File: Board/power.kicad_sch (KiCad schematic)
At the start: 19 parts, among them U2 MP2459, U3 LMR516x5

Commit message: Routing mostly done
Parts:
- added C13: 22uF/30V, Capacitor_SMD:C_0603_1608Metric, symbol Device:C_Small
- added C14, C9: 100n/100V, Capacitor_SMD:C_0603_1608Metric, symbol Device:C_Small
- added C15, C16, C8: 1µF/100V, Capacitor_SMD:C_0603_1608Metric, symbol Device:C_Small
- added D6: 1N4007, Diode_SMD:D_SOD-123, symbol Device:D_Small
- added L2: 24.5uH, symbol Device:L
- added R10: 3.48k 0.1%, Resistor_SMD:R_0603_1608Metric, symbol Device:R_Small
- added R8: 100k 0.1%, Resistor_SMD:R_0603_1608Metric, symbol Device:R_Small
- C7: value 22u -> 22uF/30V
- U3: value LMR516x5 -> LMR51635XDDCR
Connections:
- net +24V: now also C13.1, L2.2, R8.1
- net GND: now also U3.4 (GND), C13.2, C14.2, C15.2, C16.2, C8.2, R10.2
- net at U3.1 (FB): now also R10.1, R8.2
- net at U3.2 (EN): now also U3.3 (VIN), C14.1, C15.1, C16.1, C8.1, D6.1 (K)
- net at U3.5 (SW): now also C9.2, L2.1
- net at U3.6 (CB): now also C9.1
- new net VIN: D6.2 (A)
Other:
- note added: "24V SUPPLY"
- note added: "VIN range from 40V to 55V approx."
- note removed: "VIN range from 12V to 60V approx."
- moved on the sheet: C1, C11, C2, C6, C7, D1, D3, D4, D5, FB4, L1, R16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

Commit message: Schematic done.
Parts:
- removed D1: 1N4007, Diode_SMD:D_SOD-123, symbol Device:D_Small
- D6: value 1N4007 -> SE30AFBHM3/6A; footprint Diode_SMD:D_SOD-123 -> Diode_SMD:D_SMA_Handsoldering; REF SM4007PL -> SE30AFBHM3/6A
- L1: REF NLCV25T-220K-PF -> NLCV25T-220K-EFD
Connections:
- net +24V: now also C1.1, C2.1, R3.1, U2.5 (IN)
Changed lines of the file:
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@@
 	)
 	(junction
-		(at 44.45 95.25)
-		(diameter 0)
-		(color 0 0 0 0)
-	)
-	(junction
 		(at 55.88 55.88)
 		(diameter 0)
@@
 	(wire
 		(pts
-			(xy 26.67 95.25) (xy 27.94 95.25)
+			(xy 26.67 95.25) (xy 36.83 95.25)
 		)
 		(stroke
@@
 		)
 	)
+	(wire
+		(pts
+			(xy 110.49 39.37) (xy 116.84 39.37)
+		)
+		(stroke
+			(width 0)
+			(type default)
+		)
+	)
 	(polyline
 		(pts
@@
 	(wire
 		(pts
-			(xy 110.49 39.37) (xy 116.84 39.37)
-		)
-		(stroke
-			(width 0)
-			(type default)
-		)
-	)
-	(wire
-		(pts
 			(xy 165.1 101.6) (xy 167.64 101.6)
 		)
@@
 	(wire
 		(pts
-			(xy 36.83 95.25) (xy 44.45 95.25)
+			(xy 36.83 95.25) (xy 52.07 95.25)
 		)
 		(stroke
@@
 		)
 	)
-	(wire
-		(pts
-			(xy 33.02 95.25) (xy 36.83 95.25)
-		)
-		(stroke
-			(width 0)
-			(type default)
-		)
-	)
 	(polyline
 		(pts
@@
 	(wire
 		(pts
-			(xy 44.45 95.25) (xy 52.07 95.25)
-		)
-		(stroke
-			(width 0)
-			(type default)
-		)
-	)
-	(wire
-		(pts
 			(xy 64.77 48.26) (xy 64.77 55.88)
 		)
@@
 			)
 		)
-		(property "REF" "NLCV25T-220K-PF"
+		(property "REF" "NLCV25T-220K-EFD"
 			(at 127 101.6 90)
 			(effects
@@
 	)
 	(symbol
-		(lib_id "power:PWR_FLAG")
-		(at 44.45 95.25 0)
-		(unit 1)
-		(exclude_from_sim no)
-		(in_bom yes)
-		(on_board yes)
-		(dnp no)
-		(fields_autoplaced yes)
-		(property "Reference" "#FLG05"
-			(at 44.45 93.345 0)
-			(effects
-				(font
-					(size 1.27 1.27)
-				)
-				(hide yes)
-			)
-		)
-		(property "Value" "PWR_FLAG"
-			(at 44.45 91.1169 0)
-			(effects
-				(font
-					(size 1.27 1.27)
-				)
-			)
-		)
-		(property "Footprint" ""
-			(at 44.45 95.25 0)
-			(effects
-				(font
-					(size 1.27 1.27)
-				)
-				(hide yes)
-			)
-		)
-		(property "Datasheet" "~"
-			(at 44.45 95.25 0)
-			(effects
-				(font
-					(size 1.27 1.27)
-				)
-				(hide yes)
-			)
-		)
-		(property "Description" "Special symbol for telling ERC where power comes from"
-			(at 44.45 95.25 0)
-			(effects
-				(font
-					(size 1.27 1.27)
-				)
-				(hide yes)
-			)
-		)
-		(pin "1"
-		)
-		(instances
-			(project "linear_act_controller"
-				(path "/a7f12679-28d2-4dcb-a620-9ebf42b92b51/9aa0f8d5-db02-4fb8-86c3-5f9e7fcbafc5"
-					(reference "#FLG05")
-					(unit 1)
-				)
-			)
-		)
-	)
-	(symbol
 		(lib_id "Device:D_Small")
 		(at 35.56 36.83 180)
@@
 			)
 		)
-		(property "Value" "1N4007"
+		(property "Value" "SE30AFBHM3/6A"
 			(at 35.56 39.7256 0)
 			(effects
@@
 			)
 		)
-		(property "Footprint" "Diode_SMD:D_SOD-123"
+		(property "Footprint" "Diode_SMD:D_SMA_Handsoldering"
 			(at 35.56 36.83 90)
 			(effects
@@
 			)
 		)
-		(property "REF" "SM4007PL"
+		(property "REF" "SE30AFBHM3/6A"
 			(at 35.56 36.83 0)
 			(effects
@@
 					(unit 1)
 				)
-			)
-		)
-	)
-	(symbol
-		(lib_id "Device:D_Small")
-		(at 30.48 95.25 180)
-		(unit 1)
-		(exclude_from_sim no)
-		(in_bom yes)
-		(on_board yes)
-		(dnp no)
-		(property "Reference" "D1"
-			(at 30.48 100.457 0)
-			(effects
-				(font
-					(size 1.27 1.27)
-				)
-			)
-		)
-		(property "Value" "1N4007"
-			(at 30.48 98.1456 0)
-			(effects
-				(font
-					(size 1.27 1.27)
-				)
-			)
-		)
-		(property "Footprint" "Diode_SMD:D_SOD-123"
-			(at 30.48 95.25 90)
-			(effects
-				(font
-					(size 1.27 1.27)
-				)
-				(hide yes)
-			)
-		)
-		(property "Datasheet" "~"
-			(at 30.48 95.25 90)
-			(effects
-				(font
-					(size 1.27 1.27)
-				)
-				(hide yes)
-			)
-		)
-		(property "Description" "Diode, small symbol"
-			(at 30.48 95.25 0)
-			(effects
-				(font
-					(size 1.27 1.27)
-				)
-				(hide yes)
-			)
-		)
-		(property "REF" "SM4007PL"
-			(at 30.48 95.25 0)
-			(effects
-				(font
-					(size 1.27 1.27)
-				)
-				(hide yes)
-			)
-		)
-		(property "RS" ""
-			(at 30.48 95.25 0)
-			(effects
-				(font
-					(size 1.27 1.27)
-				)
-				(hide yes)
-			)
-		)
-		(property "JLCPCB" "C64898"
-			(at 30.48 95.25 0)
-			(effects
-				(font
-					(size 1.27 1.27)
-				)
-				(hide yes)
-			)
-		)
-		(property "Sim.Device" "D"
-			(at 30.48 95.25 0)
-			(effects
-				(font
-					(size 1.27 1.27)
-				)
-				(hide yes)
-			)
-		)
-		(property "Sim.Pins" "1=K 2=A"
-			(at 30.48 95.25 0)
-			(effects
-				(font
-					(size 1.27 1.27)
-				)
-				(hide yes)
-			)
-		)
-		(pin "1"
-		)
-		(pin "2"
-		)
-		(instances
-			(project "linear_act_controller"
-				(path "/a7f12679-28d2-4dcb-a620-9ebf42b92b51/9aa0f8d5-db02-4fb8-86c3-5f9e7fcbafc5"
-					(reference "D1")
-					(unit 1)
-				)

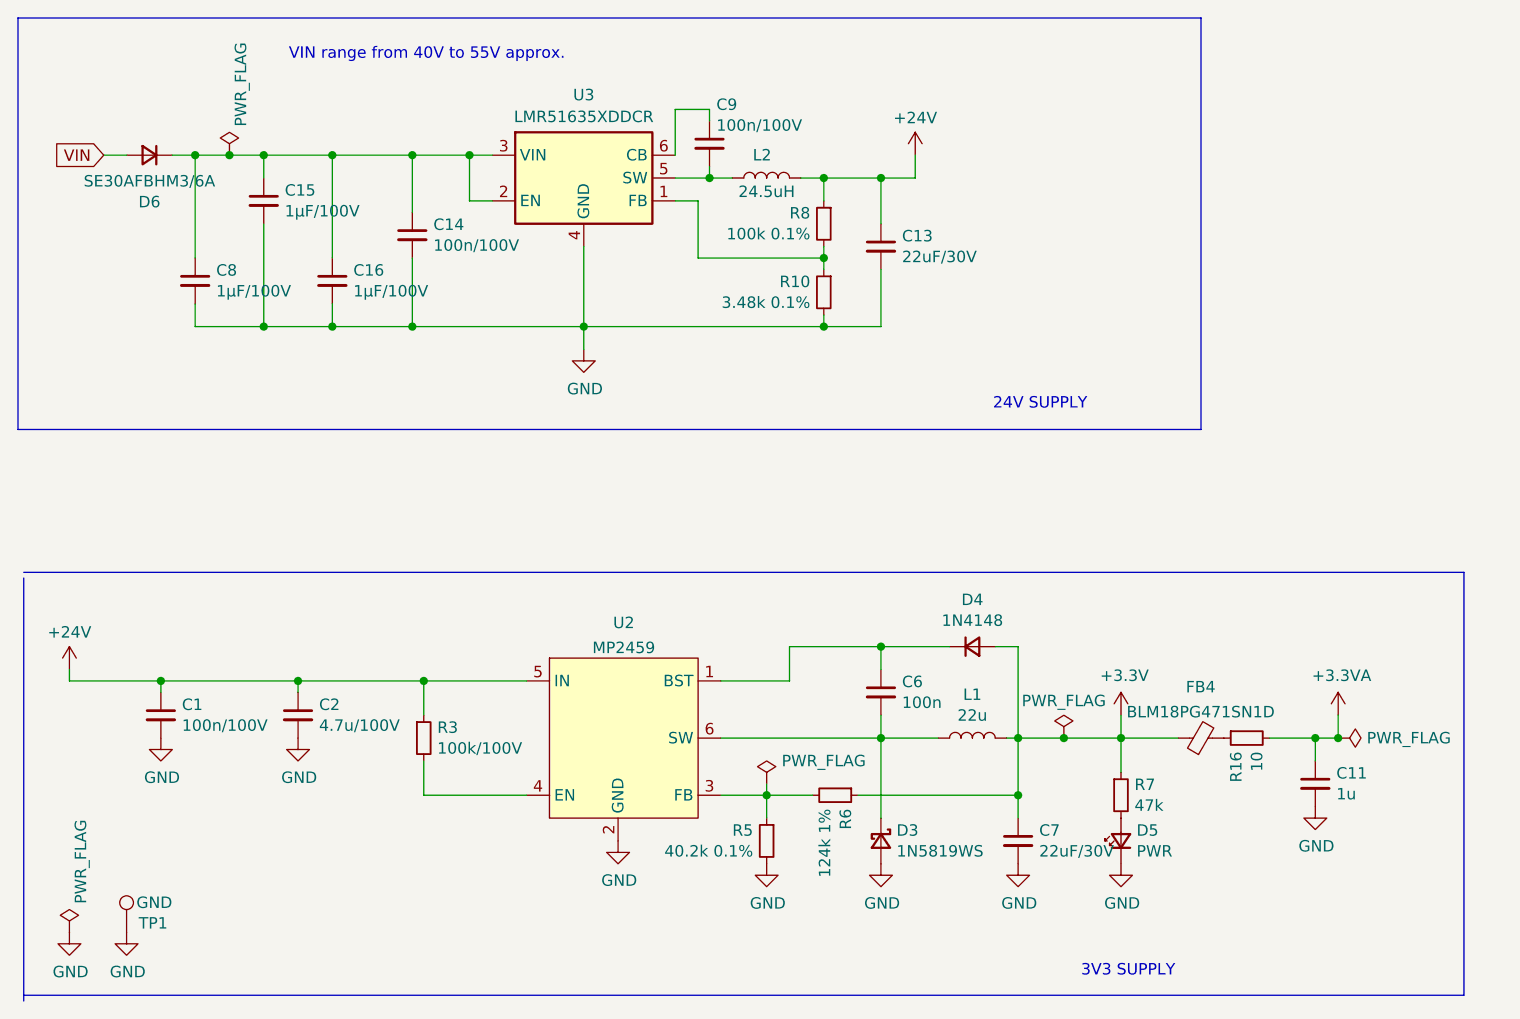
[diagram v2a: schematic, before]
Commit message: Included jdam's improvements.
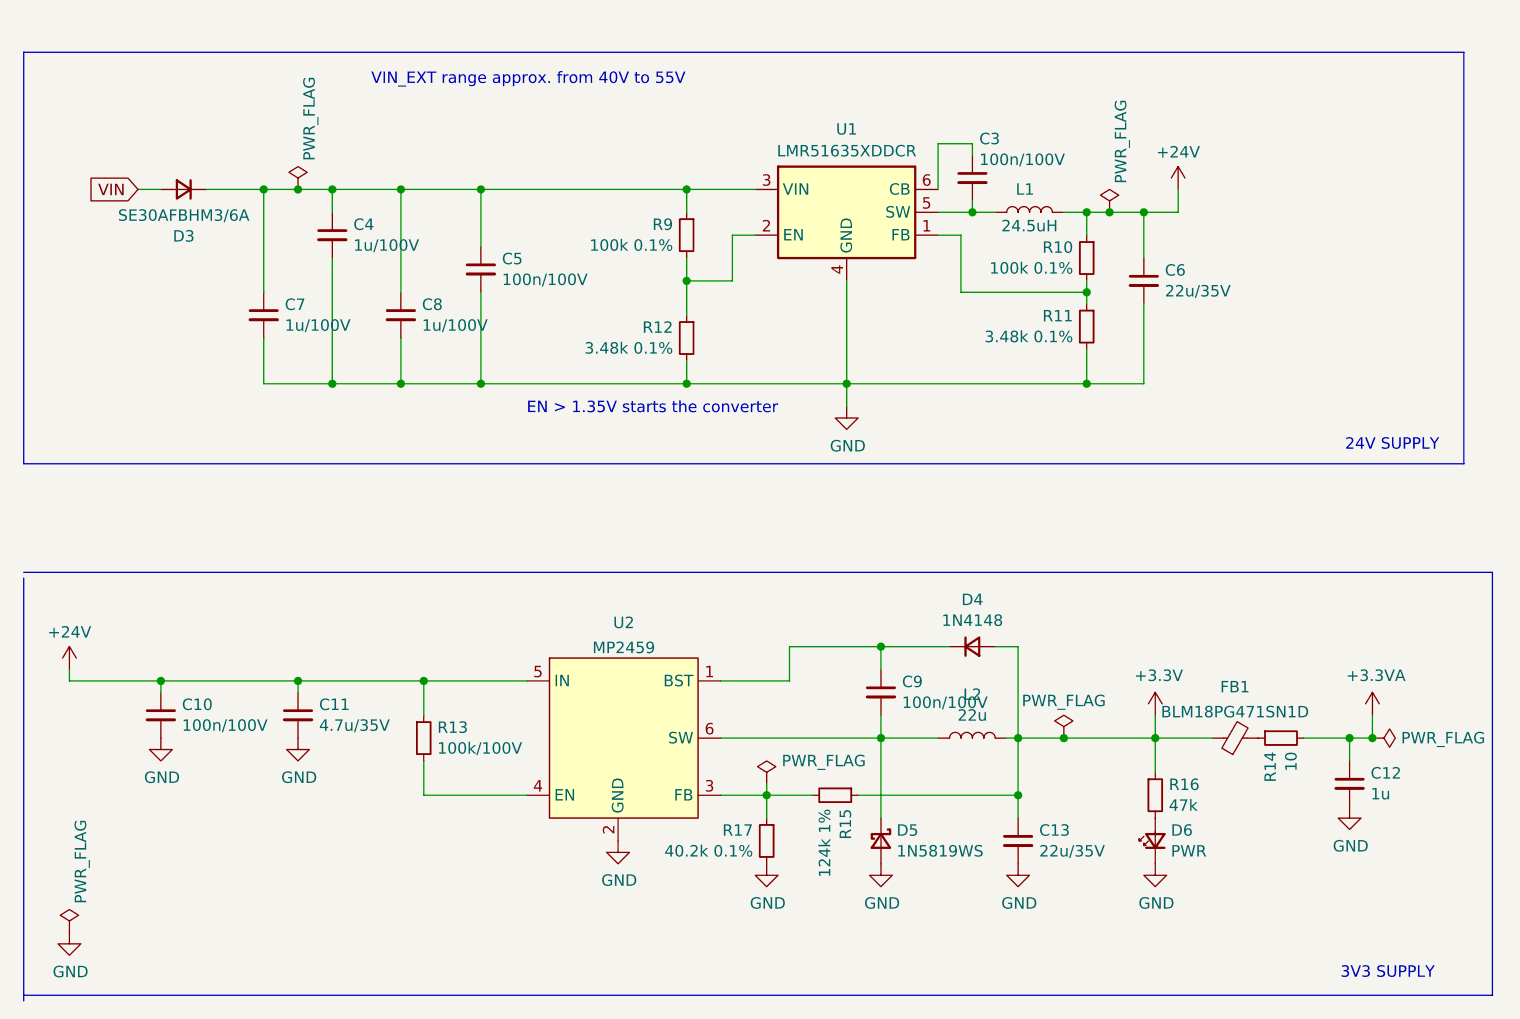
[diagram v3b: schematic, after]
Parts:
- removed TP1: GND, TestPoint:TestPoint_Pad_D1.0mm, symbol Connector:TestPoint
- added R12: 3.48k 0.1%, Resistor_SMD:R_0603_1608Metric_Pad0.98x0.95mm_HandSolder, symbol Device:R_Small
- added R9: 100k 0.1%, Resistor_SMD:R_0603_1608Metric_Pad0.98x0.95mm_HandSolder, symbol Device:R_Small
- C10: renamed from C1; footprint Capacitor_SMD:C_0603_1608Metric -> Capacitor_SMD:C_0603_1608Metric_Pad1.08x0.95mm_HandSolder
- C11: renamed from C2; value 4.7u/100V -> 4.7u/35V; footprint Capacitor_SMD:C_1206_3216Metric -> Capacitor_SMD:C_0603_1608Metric_Pad1.08x0.95mm_HandSolder; REF HMK325C7475KMHPE -> (none)
- C12: renamed from C11; footprint Capacitor_SMD:C_0603_1608Metric -> Capacitor_SMD:C_0603_1608Metric_Pad1.08x0.95mm_HandSolder
- C13: renamed from C7; value 22uF/30V -> 22u/35V; footprint Capacitor_SMD:C_1206_3216Metric -> Capacitor_SMD:C_0805_2012Metric_Pad1.18x1.45mm_HandSolder; REF JMK316AB7226KLHT -> (none)
- C3: renamed from C9; footprint Capacitor_SMD:C_0603_1608Metric -> Capacitor_SMD:C_0603_1608Metric_Pad1.08x0.95mm_HandSolder
- C4: renamed from C15; value 1µF/100V -> 1u/100V; footprint Capacitor_SMD:C_0603_1608Metric -> Capacitor_SMD:C_0603_1608Metric_Pad1.08x0.95mm_HandSolder
- C5: renamed from C14; footprint Capacitor_SMD:C_0603_1608Metric -> Capacitor_SMD:C_0603_1608Metric_Pad1.08x0.95mm_HandSolder
- C6: renamed from C13; value 22uF/30V -> 22u/35V; footprint Capacitor_SMD:C_0603_1608Metric -> Capacitor_SMD:C_0805_2012Metric_Pad1.18x1.45mm_HandSolder
- C7: renamed from C8; value 1µF/100V -> 1u/100V; footprint Capacitor_SMD:C_0603_1608Metric -> Capacitor_SMD:C_0603_1608Metric_Pad1.08x0.95mm_HandSolder
- C8: renamed from C16; value 1µF/100V -> 1u/100V; footprint Capacitor_SMD:C_0603_1608Metric -> Capacitor_SMD:C_0603_1608Metric_Pad1.08x0.95mm_HandSolder
- C9: renamed from C6; value 100n -> 100n/100V; footprint Capacitor_SMD:C_0603_1608Metric -> Capacitor_SMD:C_0603_1608Metric_Pad1.08x0.95mm_HandSolder
- D4: footprint Diode_SMD:D_SOD-323 -> Diode_SMD:D_SOD-323_HandSoldering
- D5: renamed from D3; footprint Diode_SMD:D_SOD-323 -> Diode_SMD:D_SOD-323_HandSoldering
- D6: renamed from D5; footprint LED_SMD:LED_0603_1608Metric -> LED_SMD:LED_0603_1608Metric_Pad1.05x0.95mm_HandSolder
- L1: renamed from L2; footprint (none) -> Inductors:Pulse_PG1083.253NLT
- R10: renamed from R8; footprint Resistor_SMD:R_0603_1608Metric -> Resistor_SMD:R_0603_1608Metric_Pad0.98x0.95mm_HandSolder
- R11: renamed from R10; footprint Resistor_SMD:R_0603_1608Metric -> Resistor_SMD:R_0603_1608Metric_Pad0.98x0.95mm_HandSolder
- R13: renamed from R3; footprint Resistor_SMD:R_0603_1608Metric -> Resistor_SMD:R_0603_1608Metric_Pad0.98x0.95mm_HandSolder
- R14: renamed from R16; footprint Resistor_SMD:R_0603_1608Metric -> Resistor_SMD:R_0603_1608Metric_Pad0.98x0.95mm_HandSolder
- R15: renamed from R6; footprint Resistor_SMD:R_0603_1608Metric -> Resistor_SMD:R_0603_1608Metric_Pad0.98x0.95mm_HandSolder
- R16: renamed from R7; footprint Resistor_SMD:R_0603_1608Metric -> Resistor_SMD:R_0603_1608Metric_Pad0.98x0.95mm_HandSolder
- R17: renamed from R5; footprint Resistor_SMD:R_0603_1608Metric -> Resistor_SMD:R_0603_1608Metric_Pad0.98x0.95mm_HandSolder
- renumbered D6 to D3, FB4 to FB1, L1 to L2, U3 to U1
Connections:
- net GND: now also R12.2
- net at C4.1, C5.1, C7.1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: now also R9.1; no longer U1.2 (EN)
- new net: R12.1, R9.2, U1.2 (EN)
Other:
- note added: "EN > 1.35V starts the converter"
- note added: "VIN_EXT range approx. from 40V to 55V"
- note removed: "VIN range from 40V to 55V approx."
- moved on the sheet: C12, C3, C4, C5, C6, C7, C8, D3, D6, FB1, L1, R10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

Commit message: WIP on routing
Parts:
- removed D6: PWR, LED_SMD:LED_0603_1608Metric_Pad1.05x0.95mm_HandSolder, symbol Device:LED_Small
- removed R16: 47k, Resistor_SMD:R_0603_1608Metric_Pad0.98x0.95mm_HandSolder, symbol Device:R_Small
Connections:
- net +24V: now also L1.1; no longer L1.2
- net at C3.2, U1.5 (SW): now also L1.2; no longer L1.1
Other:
- moved on the sheet: L1
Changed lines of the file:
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@@
 	(wire
 		(pts
-			(xy 147.32 101.6) (xy 147.32 105.41)
-		)
-		(stroke
-			(width 0)
-			(type default)
-		)
-	)
-	(wire
-		(pts
 			(xy 116.84 101.6) (xy 116.84 99.06)
 		)
@@
 	)
 	(symbol
-		(lib_id "power:GND")
-		(at 147.32 115.57 0)
-		(unit 1)
-		(exclude_from_sim no)
-		(in_bom yes)
-		(on_board yes)
-		(dnp no)
-		(property "Reference" "#PWR018"
-			(at 147.32 121.92 0)
-			(effects
-				(font
-					(size 1.27 1.27)
-				)
-				(hide yes)
-			)
-		)
-		(property "Value" "GND"
-			(at 147.447 119.9642 0)
-			(effects
-				(font
-					(size 1.27 1.27)
-				)
-			)
-		)
-		(property "Footprint" ""
-			(at 147.32 115.57 0)
-			(effects
-				(font
-					(size 1.27 1.27)
-				)
-				(hide yes)
-			)
-		)
-		(property "Datasheet" ""
-			(at 147.32 115.57 0)
-			(effects
-				(font
-					(size 1.27 1.27)
-				)
-				(hide yes)
-			)
-		)
-		(property "Description" "Power symbol creates a global label with name \"GND\" , ground"
-			(at 147.32 115.57 0)
-			(effects
-				(font
-					(size 1.27 1.27)
-				)
-				(hide yes)
-			)
-		)
-		(pin "1"
-		)
-		(instances
-			(project "linear_act_controller"
-				(path "/a7f12679-28d2-4dcb-a620-9ebf42b92b51/9aa0f8d5-db02-4fb8-86c3-5f9e7fcbafc5"
-					(reference "#PWR018")
-					(unit 1)
-				)
-			)
-		)
-	)
-	(symbol
 		(lib_id "power:PWR_FLAG")
 		(at 142.24 43.18 0)
@@
 	(symbol
 		(lib_id "Device:L")
-		(at 133.35 43.18 90)
+		(at 133.35 43.18 270)
 		(unit 1)
 		(exclude_from_sim no)
@@
 		(dnp no)
 		(property "Reference" "L1"
-			(at 132.842 40.64 90)
+			(at 133.35 45.212 90)
 			(effects
 				(font
@@
 		)
 		(property "Value" "24.5uH"
-			(at 133.35 44.704 90)
+			(at 133.35 41.656 90)
 			(effects
 				(font
@@
 	)
 	(symbol
-		(lib_id "Device:R_Small")
-		(at 147.32 107.95 0)
-		(unit 1)
-		(exclude_from_sim no)
-		(in_bom yes)
-		(on_board yes)
-		(dnp no)
-		(property "Reference" "R16"
-			(at 148.8186 106.7816 0)
-			(effects
-				(font
-					(size 1.27 1.27)
-				)
-				(justify left)
-			)
-		)
-		(property "Value" "47k"
-			(at 148.8186 109.093 0)
-			(effects
-				(font
-					(size 1.27 1.27)
-				)
-				(justify left)
-			)
-		)
-		(property "Footprint" "Resistor_SMD:R_0603_1608Metric_Pad0.98x0.95mm_HandSolder"
-			(at 147.32 107.95 0)
-			(effects
-				(font
-					(size 1.27 1.27)
-				)
-				(hide yes)
-			)
-		)
-		(property "Datasheet" "~"
-			(at 147.32 107.95 0)
-			(effects
-				(font
-					(size 1.27 1.27)
-				)
-				(hide yes)
-			)
-		)
-		(property "Description" "Resistor, small symbol"
-			(at 147.32 107.95 0)
-			(effects
-				(font
-					(size 1.27 1.27)
-				)
-				(hide yes)
-			)
-		)
-		(pin "1"
-		)
-		(pin "2"
-		)
-		(instances
-			(project "linear_act_controller"
-				(path "/a7f12679-28d2-4dcb-a620-9ebf42b92b51/9aa0f8d5-db02-4fb8-86c3-5f9e7fcbafc5"
-					(reference "R16")
-					(unit 1)
-				)
-			)
-		)
-	)
-	(symbol
 		(lib_id "Device:C_Small")
 		(at 127 39.37 0)
@@
 					(unit 1)
 				)
-			)
-		)
-	)
-	(symbol
-		(lib_id "Device:LED_Small")
-		(at 147.32 113.03 90)
-		(unit 1)
-		(exclude_from_sim no)
-		(in_bom yes)
-		(on_board yes)
-		(dnp no)
-		(property "Reference" "D6"
-			(at 149.0472 111.8616 90)
-			(effects
-				(font
-					(size 1.27 1.27)
-				)
-				(justify right)
-			)
-		)
-		(property "Value" "PWR"
-			(at 149.0472 114.173 90)
-			(effects
-				(font
-					(size 1.27 1.27)
-				)
-				(justify right)
-			)
-		)
-		(property "Footprint" "LED_SMD:LED_0603_1608Metric_Pad1.05x0.95mm_HandSolder"
-			(at 147.32 113.03 90)
-			(effects
-				(font
-					(size 1.27 1.27)
-				)
-				(hide yes)
-			)
-		)
-		(property "Datasheet" "~"
-			(at 147.32 113.03 90)
-			(effects
-				(font
-					(size 1.27 1.27)
-				)
-				(hide yes)
-			)
-		)
-		(property "Description" "Light emitting diode, small symbol"
-			(at 147.32 113.03 0)
-			(effects
-				(font
-					(size 1.27 1.27)
-				)
-				(hide yes)
-			)
-		)
-		(property "Sim.Pin" "1=K 2=A"
-			(at 147.32 113.03 0)
-			(effects
-				(font
-					(size 1.27 1.27)
-				)
-				(hide yes)
-			)
-		)
-		(pin "1"
-		)
-		(pin "2"
-		)
-		(instances
-			(project "linear_act_controller"
-				(path "/a7f12679-28d2-4dcb-a620-9ebf42b92b51/9aa0f8d5-db02-4fb8-86c3-5f9e7fcbafc5"
-					(reference "D6")
-					(unit 1)
-				)

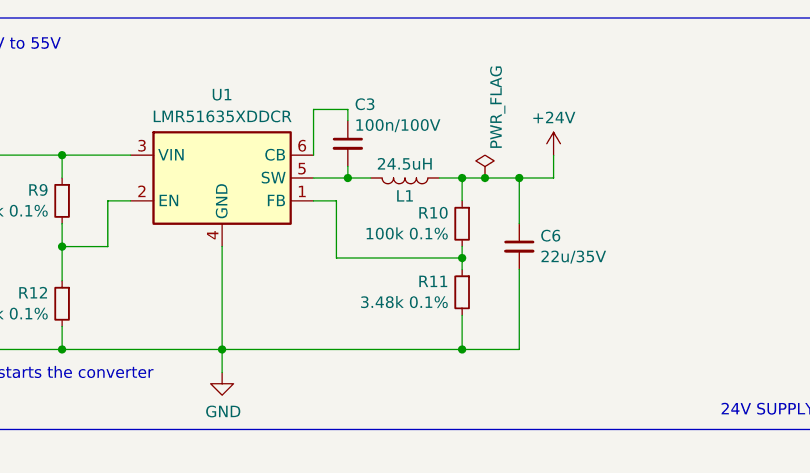
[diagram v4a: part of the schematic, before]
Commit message: Routing done, before adding polyfuse
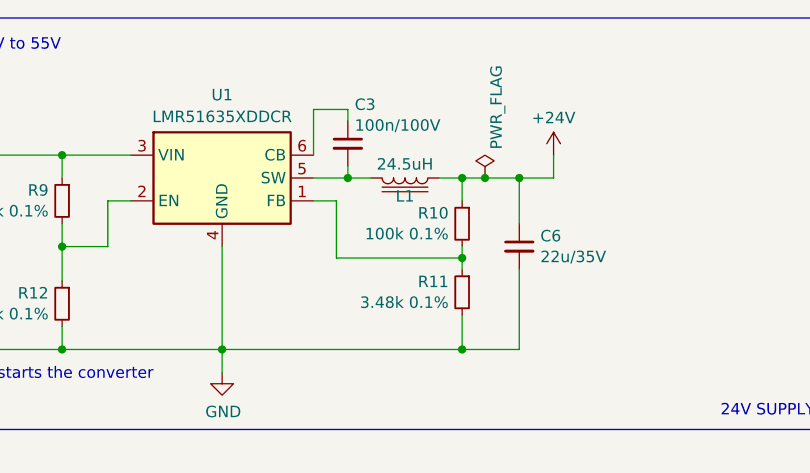
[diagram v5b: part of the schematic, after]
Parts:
- L1: symbol Device:L -> Device:L_Iron
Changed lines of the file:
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@@
 	)
 	(symbol
-		(lib_id "Device:L")
+		(lib_id "Device:L_Iron")
 		(at 133.35 43.18 270)
 		(unit 1)
@@
 			)
 		)
-		(property "Description" "Inductor"
+		(property "Description" "Inductor with iron core"
 			(at 133.35 43.18 0)
 			(effects
